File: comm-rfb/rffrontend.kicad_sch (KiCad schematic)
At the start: 18 parts, among them U2 SKY67150-396LF

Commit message: comm-rfb: reduce number of sheets in schematic
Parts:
- removed J? (x2): Conn_Coaxial, Connector_Coaxial:SMA_Amphenol_132134-10_Vertical, symbol Connector:Conn_Coaxial
- added J6, J9: Conn_Coaxial, Connector_Coaxial:SMA_Amphenol_132134-10_Vertical, symbol Connector:Conn_Coaxial
- C1, C2, C3, C4, C5, C6, C7: footprint (none) -> Capacitor_SMD:C_0402_1005Metric
- C8: value 1.8p -> 1p8; footprint (none) -> Capacitor_SMD:C_0402_1005Metric
- J7, J8: renamed from J?; value Conn_Coaxial -> (none); footprint Connector_Coaxial:SMA_Amphenol_132134-10_Vertical -> (none)
- L1, L2: footprint (none) -> Inductor_SMD:L_0402_1005Metric
- R1: footprint (none) -> Resistor_SMD:R_0603_1608Metric
- R2, R3: footprint (none) -> Resistor_SMD:R_0402_1005Metric
- U2: value SKY67150-396LF -> (none); footprint SON50P200X200X80-9N -> (none)
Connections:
- net AMP-TO-EXT: now also J9.1 (In)
- net EM-TO-AMP: now also J6.1 (In)
- net GND: now also J6.2 (Ext), J9.2 (Ext)
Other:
- moved on the sheet: C1, C2, C3, C4, C5, C6, C7, C8, J7, J8, L1, L2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

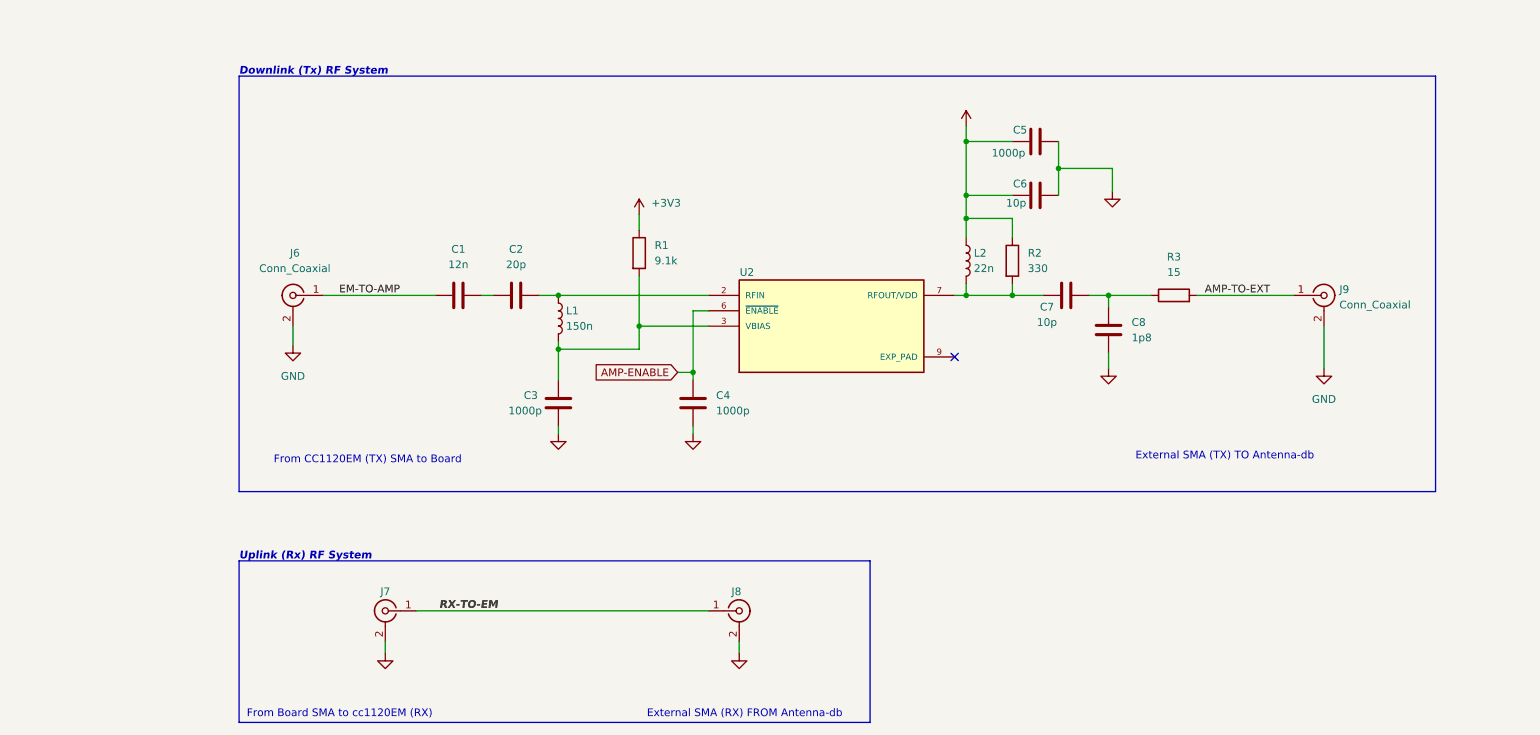
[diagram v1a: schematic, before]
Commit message: comm-rfb: reformat for rebase
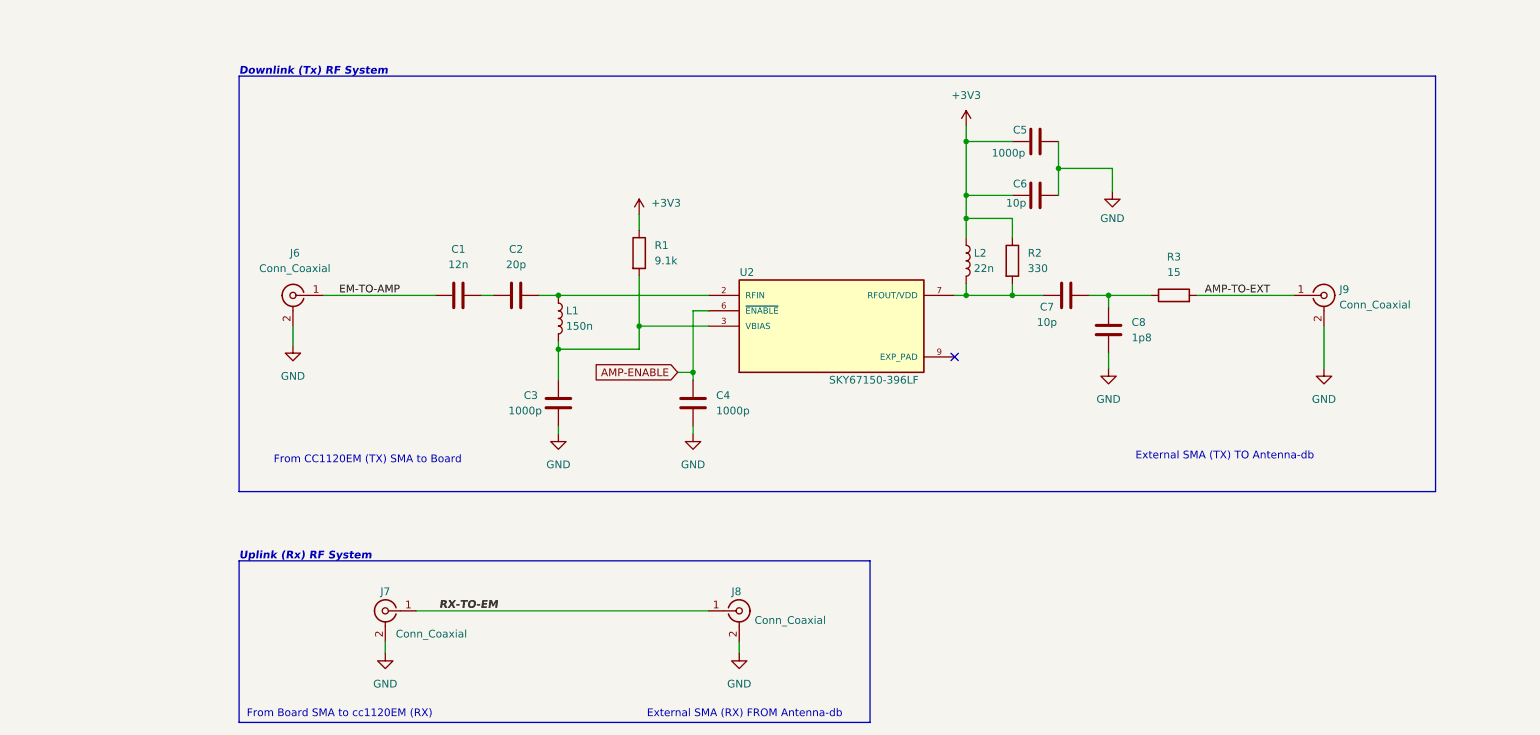
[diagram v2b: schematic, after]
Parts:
- J7, J8: value (none) -> Conn_Coaxial; footprint (none) -> Connector_Coaxial:SMA_Amphenol_132134-10_Vertical
- U2: value (none) -> SKY67150-396LF; footprint (none) -> SON50P200X200X80-9N
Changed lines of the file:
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@@
       (effects (font (size 1.27 1.27)) hide)
     )
-    (property "Value" "" (id 1) (at 108.585 90.17 0))
+    (property "Value" "GND" (id 1) (at 108.585 90.17 0))
     (property "Footprint" "" (id 2) (at 108.585 85.09 0)
       (effects (font (size 1.27 1.27)) hide)
@@
       (effects (font (size 1.27 1.27)) hide)
     )
-    (property "Value" "" (id 1) (at 200.025 49.53 0))
+    (property "Value" "GND" (id 1) (at 200.025 49.53 0))
     (property "Footprint" "" (id 2) (at 200.025 45.085 0)
       (effects (font (size 1.27 1.27)) hide)
@@
       (effects (font (size 1.27 1.27)) hide)
     )
-    (property "Value" "" (id 1) (at 199.39 79.375 0))
+    (property "Value" "GND" (id 1) (at 199.39 79.375 0))
     (property "Footprint" "" (id 2) (at 199.39 74.295 0)
       (effects (font (size 1.27 1.27)) hide)
@@
       (effects (font (size 1.27 1.27)) hide)
     )
-    (property "Value" "" (id 1) (at 130.81 90.17 0))
+    (property "Value" "GND" (id 1) (at 130.81 90.17 0))
     (property "Footprint" "" (id 2) (at 130.81 85.09 0)
       (effects (font (size 1.27 1.27)) hide)
@@
       (effects (font (size 1.27 1.27)) hide)
     )
-    (property "Value" "" (id 1) (at 175.895 29.21 0))
+    (property "Value" "+3V3" (id 1) (at 175.895 29.21 0))
     (property "Footprint" "" (id 2) (at 175.895 34.29 0)
       (effects (font (size 1.27 1.27)) hide)
@@
       (effects (font (size 1.27 1.27)) (justify left))
     )
-    (property "Value" "" (id 1) (at 140.97 115.8631 0)
-      (effects (font (size 1.27 1.27)) (justify left))
-    )
-    (property "Footprint" "" (id 2) (at 138.43 114.3 0)
+    (property "Value" "Conn_Coaxial" (id 1) (at 140.97 115.8631 0)
+      (effects (font (size 1.27 1.27)) (justify left))
+    )
+    (property "Footprint" "Connector_Coaxial:SMA_Amphenol_132134-10_Vertical" (id 2) (at 138.43 114.3 0)
       (effects (font (size 1.27 1.27)) hide)
     )
@@
     (in_bom yes) (on_board yes)
     (property "Reference" "U2" (id 0) (at 139.7 58.42 0))
-    (property "Value" "" (id 1) (at 160.655 76.2 0))
-    (property "Footprint" "" (id 2) (at 153.67 67.31 0)
+    (property "Value" "SKY67150-396LF" (id 1) (at 160.655 76.2 0))
+    (property "Footprint" "SON50P200X200X80-9N" (id 2) (at 153.67 67.31 0)
       (effects (font (size 1.27 1.27)) (justify bottom) hide)
     )
@@
       (effects (font (size 1.27 1.27)) hide)
     )
-    (property "Value" "" (id 1) (at 138.43 126.365 0))
+    (property "Value" "GND" (id 1) (at 138.43 126.365 0))
     (property "Footprint" "" (id 2) (at 138.43 121.285 0)
       (effects (font (size 1.27 1.27)) hide)
@@
     (in_bom yes) (on_board yes)
     (property "Reference" "J7" (id 0) (at 80.01 111.125 0))
-    (property "Value" "" (id 1) (at 87.63 118.11 0))
-    (property "Footprint" "" (id 2) (at 80.01 114.3 0)
+    (property "Value" "Conn_Coaxial" (id 1) (at 87.63 118.11 0))
+    (property "Footprint" "Connector_Coaxial:SMA_Amphenol_132134-10_Vertical" (id 2) (at 80.01 114.3 0)
       (effects (font (size 1.27 1.27)) hide)
     )
@@
       (effects (font (size 1.27 1.27)) hide)
     )
-    (property "Value" "" (id 1) (at 80.01 126.365 0))
+    (property "Value" "GND" (id 1) (at 80.01 126.365 0))
     (property "Footprint" "" (id 2) (at 80.01 121.285 0)
       (effects (font (size 1.27 1.27)) hide)

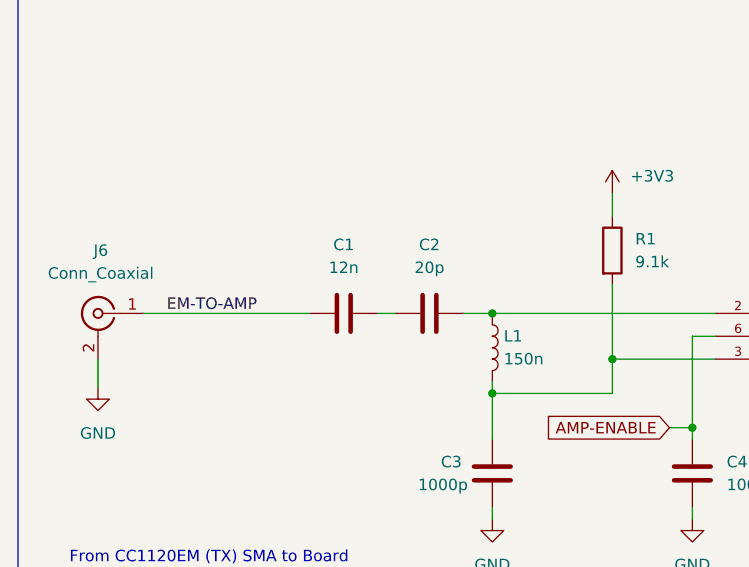
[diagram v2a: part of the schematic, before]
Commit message: comm-rfb: include correct spacing for cc1120-em connectors, remove traces
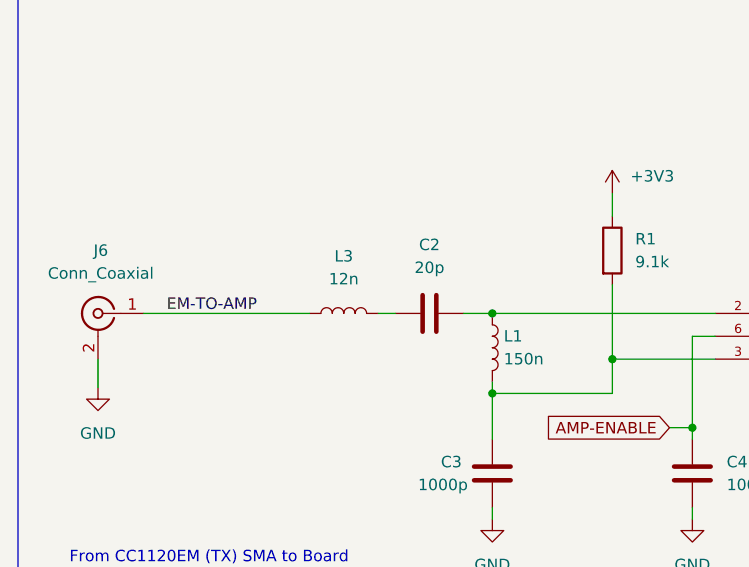
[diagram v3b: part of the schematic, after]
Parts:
- removed C1: 12n, Capacitor_SMD:C_0402_1005Metric, symbol Device:C
- added L3: 12n, Inductor_SMD:L_0402_1005Metric, symbol Device:L
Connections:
- net EM-TO-AMP: now also L3.1
- net at C2.1: now also L3.2
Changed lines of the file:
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@@
     (pin "2")
   )
-  (symbol (lib_id "Device:C") (at 92.075 62.23 270) (unit 1)
+  (symbol (lib_id "Device:L") (at 92.075 62.23 90) (unit 1)
     (in_bom yes) (on_board yes) (fields_autoplaced)
-    (property "Reference" "C1" (id 0) (at 92.075 54.61 90))
-    (property "Value" "12n" (id 1) (at 92.075 57.15 90))
-    (property "Footprint" "Capacitor_SMD:C_0402_1005Metric" (id 2) (at 88.265 63.1952 0)
+    (property "Reference" "L3" (id 0) (at 92.075 55.88 90))
+    (property "Value" "12n" (id 1) (at 92.075 58.42 90))
+    (property "Footprint" "Inductor_SMD:L_0402_1005Metric" (id 2) (at 92.075 62.23 0)
       (effects (font (size 1.27 1.27)) hide)
     )

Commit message: comm-rfb: finish RF front end
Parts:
- J6, J7: footprint Connector_Coaxial:SMA_Amphenol_132134-10_Vertical -> Connector_Coaxial:U.FL_Hirose_U.FL-R-SMT-1_Vertical
- J8, J9: footprint Connector_Coaxial:SMA_Amphenol_132134-10_Vertical -> Connector_Coaxial:SMA_Amphenol_132134-11_Vertical
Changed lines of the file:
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@@
       (effects (font (size 1.27 1.27)) (justify left))
     )
-    (property "Footprint" "Connector_Coaxial:SMA_Amphenol_132134-10_Vertical" (id 2) (at 234.95 62.23 0)
+    (property "Footprint" "Connector_Coaxial:SMA_Amphenol_132134-11_Vertical" (id 2) (at 234.95 62.23 0)
       (effects (font (size 1.27 1.27)) hide)
     )
@@
     (property "Reference" "J6" (id 0) (at 65.0874 55.245 0))
     (property "Value" "Conn_Coaxial" (id 1) (at 65.0874 57.785 0))
-    (property "Footprint" "Connector_Coaxial:SMA_Amphenol_132134-10_Vertical" (id 2) (at 64.77 62.23 0)
+    (property "Footprint" "Connector_Coaxial:U.FL_Hirose_U.FL-R-SMT-1_Vertical" (id 2) (at 64.77 62.23 0)
       (effects (font (size 1.27 1.27)) hide)
     )
@@
       (effects (font (size 1.27 1.27)) (justify left))
     )
-    (property "Footprint" "Connector_Coaxial:SMA_Amphenol_132134-10_Vertical" (id 2) (at 138.43 114.3 0)
+    (property "Footprint" "Connector_Coaxial:SMA_Amphenol_132134-11_Vertical" (id 2) (at 138.43 114.3 0)
       (effects (font (size 1.27 1.27)) hide)
     )
@@
     (property "Reference" "J7" (id 0) (at 80.01 111.125 0))
     (property "Value" "Conn_Coaxial" (id 1) (at 87.63 118.11 0))
-    (property "Footprint" "Connector_Coaxial:SMA_Amphenol_132134-10_Vertical" (id 2) (at 80.01 114.3 0)
-      (effects (font (size 1.27 1.27)) hide)
-    )
+    (property "Footprint" "Connector_Coaxial:U.FL_Hirose_U.FL-R-SMT-1_Vertical" (id 2) (at 80.01 114.3 0)
+      (effects (font (size 1.27 1.27)) hide)
+    )
